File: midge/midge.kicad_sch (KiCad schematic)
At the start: 18 parts, among them SW1 SW_PUSH, SW10 SW_PUSH, SW11 SW_PUSH, SW12 SW_PUSH, SW13 SW_PUSH, SW14 SW_PUSH, SW15 SW_PUSH, SW2 SW_PUSH, SW3 SW_PUSH, SW4 SW_PUSH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

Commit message: Renamed Knott to Midge.
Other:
- title: Knott -> Midge
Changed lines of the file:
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@@
   (paper "A4")
   (title_block
-    (title "Knott")
-    (date "2021-08-18")
-    (rev "0.1")
+    (title "Midge")
+    (date "2021-09-20")
+    (rev "0.2.1")
     (company "jmnw")
   )

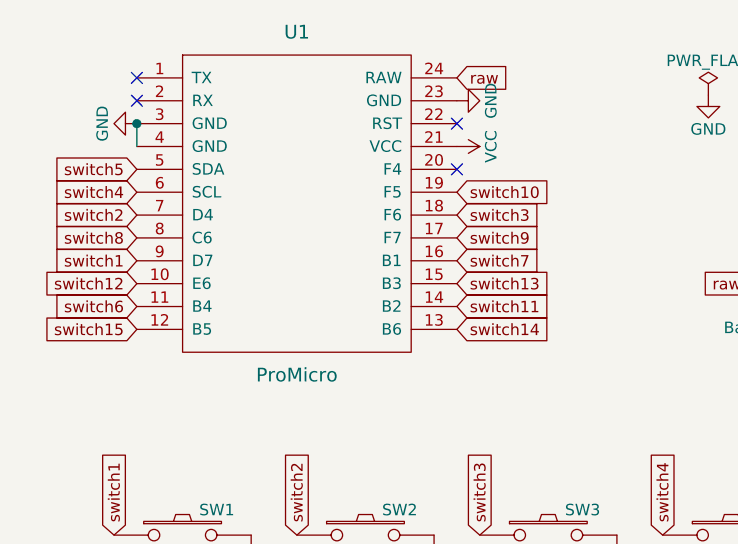
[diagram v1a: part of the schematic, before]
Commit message: Updated the Midge to the jumper pro micro footprint, breaking the pin order.
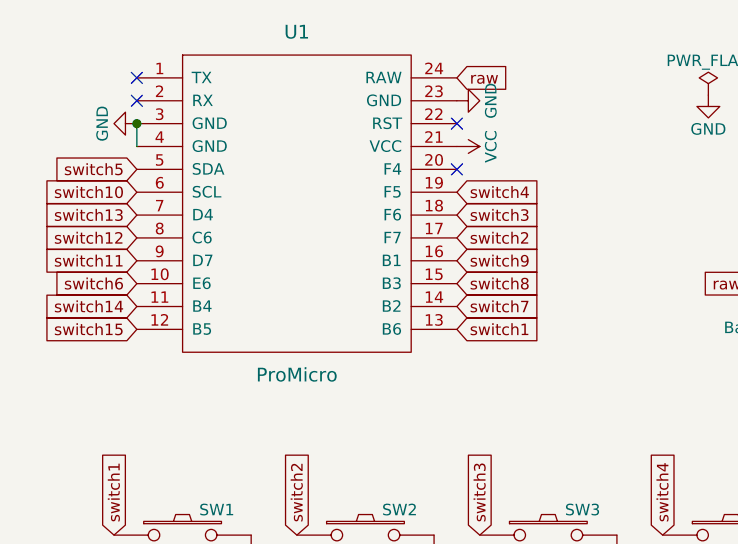
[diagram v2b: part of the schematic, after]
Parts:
- U1: footprint bugs:ProMicro_reversible -> bugs:ProMicro_jumpers
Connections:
- net switch1: now also U1.13 (B6); no longer U1.9 (D7)
- net switch10: now also U1.6 (SCL); no longer U1.19 (F5)
- net switch11: now also U1.9 (D7); no longer U1.14 (B2)
- net switch12: now also U1.8 (C6); no longer U1.10 (E6)
- net switch13: now also U1.7 (D4); no longer U1.15 (B3)
- net switch14: now also U1.11 (B4); no longer U1.13 (B6)
- net switch2: now also U1.17 (F7); no longer U1.7 (D4)
- net switch4: now also U1.19 (F5); no longer U1.6 (SCL)
- net switch6: now also U1.10 (E6); no longer U1.11 (B4)
- net switch7: now also U1.14 (B2); no longer U1.16 (B1)
- net switch8: now also U1.15 (B3); no longer U1.8 (C6)
- net switch9: now also U1.16 (B1); no longer U1.17 (F7)
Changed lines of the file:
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@@
     )
   )
-  (global_label "switch4" (shape input) (at 41.91 46.99 180) (fields_autoplaced)
+  (global_label "switch10" (shape input) (at 41.91 46.99 180) (fields_autoplaced)
     (effects (font (size 1.27 1.27)) (justify right))
-    (property "Intersheet References" "${INTERSHEET_REFS}" (id 0) (at 32.5004 46.9106 0)
+    (property "Intersheet References" "${INTERSHEET_REFS}" (id 0) (at 31.2909 47.0694 0)
       (effects (font (size 1.27 1.27)) (justify right) hide)
     )
   )
-  (global_label "switch2" (shape input) (at 41.91 49.53 180) (fields_autoplaced)
+  (global_label "switch13" (shape input) (at 41.91 49.53 180) (fields_autoplaced)
     (effects (font (size 1.27 1.27)) (justify right))
-    (property "Intersheet References" "${INTERSHEET_REFS}" (id 0) (at 32.5004 49.4506 0)
+    (property "Intersheet References" "${INTERSHEET_REFS}" (id 0) (at 31.2909 49.6094 0)
       (effects (font (size 1.27 1.27)) (justify right) hide)
     )
   )
-  (global_label "switch8" (shape input) (at 41.91 52.07 180) (fields_autoplaced)
+  (global_label "switch12" (shape input) (at 41.91 52.07 180) (fields_autoplaced)
     (effects (font (size 1.27 1.27)) (justify right))
-    (property "Intersheet References" "${INTERSHEET_REFS}" (id 0) (at 32.5004 51.9906 0)
+    (property "Intersheet References" "${INTERSHEET_REFS}" (id 0) (at 31.2909 52.1494 0)
       (effects (font (size 1.27 1.27)) (justify right) hide)
     )
   )
-  (global_label "switch1" (shape input) (at 41.91 54.61 180) (fields_autoplaced)
+  (global_label "switch11" (shape input) (at 41.91 54.61 180) (fields_autoplaced)
     (effects (font (size 1.27 1.27)) (justify right))
-    (property "Intersheet References" "${INTERSHEET_REFS}" (id 0) (at 32.5004 54.5306 0)
+    (property "Intersheet References" "${INTERSHEET_REFS}" (id 0) (at 31.2909 54.6894 0)
       (effects (font (size 1.27 1.27)) (justify right) hide)
     )
   )
-  (global_label "switch12" (shape input) (at 41.91 57.15 180) (fields_autoplaced)
+  (global_label "switch6" (shape input) (at 41.91 57.15 180) (fields_autoplaced)
     (effects (font (size 1.27 1.27)) (justify right))
-    (property "Intersheet References" "${INTERSHEET_REFS}" (id 0) (at 31.2909 57.2294 0)
+    (property "Intersheet References" "${INTERSHEET_REFS}" (id 0) (at 32.5004 57.0706 0)
       (effects (font (size 1.27 1.27)) (justify right) hide)
     )
   )
-  (global_label "switch6" (shape input) (at 41.91 59.69 180) (fields_autoplaced)
+  (global_label "switch14" (shape input) (at 41.91 59.69 180) (fields_autoplaced)
     (effects (font (size 1.27 1.27)) (justify right))
-    (property "Intersheet References" "${INTERSHEET_REFS}" (id 0) (at 32.5004 59.6106 0)
+    (property "Intersheet References" "${INTERSHEET_REFS}" (id 0) (at 31.2909 59.7694 0)
       (effects (font (size 1.27 1.27)) (justify right) hide)
     )
@@
     )
   )
-  (global_label "switch10" (shape input) (at 77.47 46.99 0) (fields_autoplaced)
-    (effects (font (size 1.27 1.27)) (justify left))
-    (property "Intersheet References" "${INTERSHEET_REFS}" (id 0) (at 88.0891 46.9106 0)
+  (global_label "switch4" (shape input) (at 77.47 46.99 0) (fields_autoplaced)
+    (effects (font (size 1.27 1.27)) (justify left))
+    (property "Intersheet References" "${INTERSHEET_REFS}" (id 0) (at 86.8796 47.0694 0)
       (effects (font (size 1.27 1.27)) (justify left) hide)
     )
@@
     )
   )
-  (global_label "switch9" (shape input) (at 77.47 52.07 0) (fields_autoplaced)
-    (effects (font (size 1.27 1.27)) (justify left))
-    (property "Intersheet References" "${INTERSHEET_REFS}" (id 0) (at 86.8796 51.9906 0)
-      (effects (font (size 1.27 1.27)) (justify left) hide)
-    )
-  )
-  (global_label "switch7" (shape input) (at 77.47 54.61 0) (fields_autoplaced)
-    (effects (font (size 1.27 1.27)) (justify left))
-    (property "Intersheet References" "${INTERSHEET_REFS}" (id 0) (at 86.8796 54.6894 0)
-      (effects (font (size 1.27 1.27)) (justify left) hide)
-    )
-  )
-  (global_label "switch13" (shape input) (at 77.47 57.15 0) (fields_autoplaced)
-    (effects (font (size 1.27 1.27)) (justify left))
-    (property "Intersheet References" "${INTERSHEET_REFS}" (id 0) (at 88.0891 57.0706 0)
-      (effects (font (size 1.27 1.27)) (justify left) hide)
-    )
-  )
-  (global_label "switch11" (shape input) (at 77.47 59.69 0) (fields_autoplaced)
-    (effects (font (size 1.27 1.27)) (justify left))
-    (property "Intersheet References" "${INTERSHEET_REFS}" (id 0) (at 88.0891 59.6106 0)
-      (effects (font (size 1.27 1.27)) (justify left) hide)
-    )
-  )
-  (global_label "switch14" (shape input) (at 77.47 62.23 0) (fields_autoplaced)
-    (effects (font (size 1.27 1.27)) (justify left))
-    (property "Intersheet References" "${INTERSHEET_REFS}" (id 0) (at 88.0891 62.1506 0)
+  (global_label "switch2" (shape input) (at 77.47 52.07 0) (fields_autoplaced)
+    (effects (font (size 1.27 1.27)) (justify left))
+    (property "Intersheet References" "${INTERSHEET_REFS}" (id 0) (at 86.8796 52.1494 0)
+      (effects (font (size 1.27 1.27)) (justify left) hide)
+    )
+  )
+  (global_label "switch9" (shape input) (at 77.47 54.61 0) (fields_autoplaced)
+    (effects (font (size 1.27 1.27)) (justify left))
+    (property "Intersheet References" "${INTERSHEET_REFS}" (id 0) (at 86.8796 54.5306 0)
+      (effects (font (size 1.27 1.27)) (justify left) hide)
+    )
+  )
+  (global_label "switch8" (shape input) (at 77.47 57.15 0) (fields_autoplaced)
+    (effects (font (size 1.27 1.27)) (justify left))
+    (property "Intersheet References" "${INTERSHEET_REFS}" (id 0) (at 86.8796 57.2294 0)
+      (effects (font (size 1.27 1.27)) (justify left) hide)
+    )
+  )
+  (global_label "switch7" (shape input) (at 77.47 59.69 0) (fields_autoplaced)
+    (effects (font (size 1.27 1.27)) (justify left))
+    (property "Intersheet References" "${INTERSHEET_REFS}" (id 0) (at 86.8796 59.7694 0)
+      (effects (font (size 1.27 1.27)) (justify left) hide)
+    )
+  )
+  (global_label "switch1" (shape input) (at 77.47 62.23 0) (fields_autoplaced)
+    (effects (font (size 1.27 1.27)) (justify left))
+    (property "Intersheet References" "${INTERSHEET_REFS}" (id 0) (at 86.8796 62.3094 0)
       (effects (font (size 1.27 1.27)) (justify left) hide)
     )
@@
       (effects (font (size 1.524 1.524)))
     )
-    (property "Footprint" "bugs:ProMicro_reversible" (id 2) (at 62.23 80.01 0)
+    (property "Footprint" "bugs:ProMicro_jumpers" (id 2) (at 62.23 80.01 0)
       (effects (font (size 1.524 1.524)) hide)
     )
@@
     )
     (path "/00000000-0000-0000-0000-00005a5e14c2"
-      (reference "U1") (unit 1) (value "ProMicro") (footprint "bugs:ProMicro_reversible")
-    )
-  )
+      (reference "U1") (unit 1) (value "ProMicro") (footprint "bugs:ProMicro_jumpers")
+    )
+  )
